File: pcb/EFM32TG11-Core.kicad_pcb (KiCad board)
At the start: 2 copper layers, 76.2 x 45.7 mm, 53 parts, among them J1 PWR_IN, J2 EXT_PWR, J3 EXT_UART, J4 EXT_I2C, J5 BOOT, J6 Conn_ARM_JTAG_SWD_10, J7 GPIO_HI, J8 GPIO_LO, Q1 Si2301CDS, SW1 SW_Push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

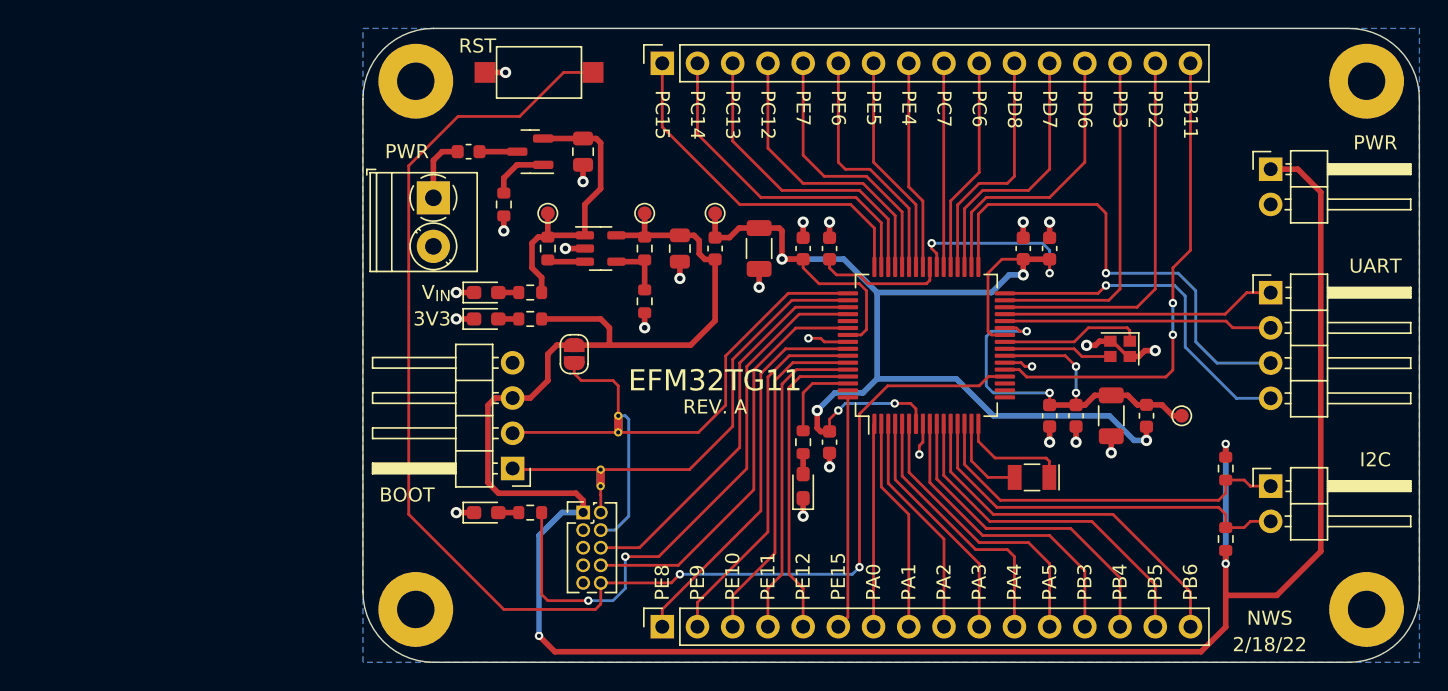
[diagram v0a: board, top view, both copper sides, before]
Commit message: Reorganization of schematic to heirarchical sheets
Took single sheet schematic and reorganized to 3 heirarchical sheets.
This allowed for the schematic to be printable on 8.5"x11" sheets of
paper without losing clarity of the schematic. All reference
designators were maintained.

Buses and interconnects between pages still need to be added to the
schematic to finish transition.

[Issue: X]
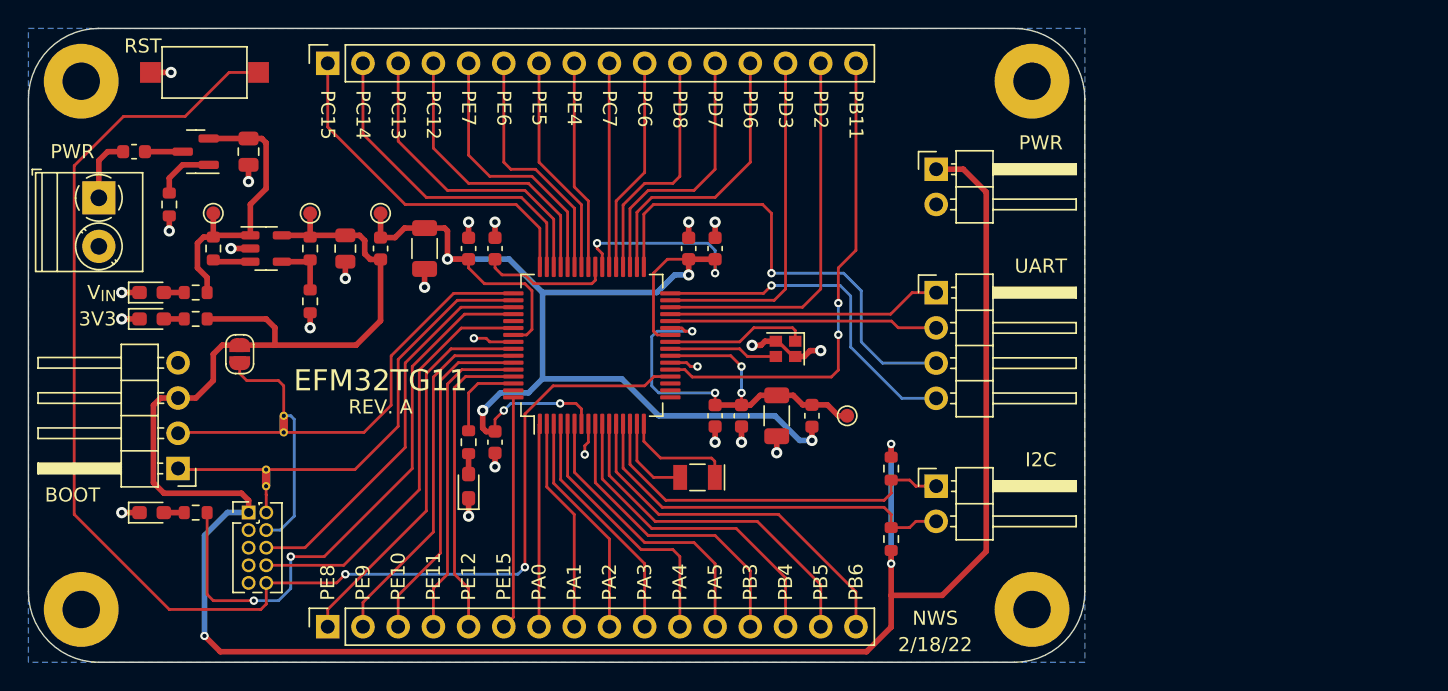
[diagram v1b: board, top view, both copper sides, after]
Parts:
- J7: value GPIO_HI -> GPIO_LO
- J8: value GPIO_LO -> GPIO_HI
- R10, R9: value 4.7k -> 4k7
- R2, R4, R7, R8: value 2.2k -> 2k2
- R3: value 2.0M -> 2M
- R6: value 1.2M -> 1M2
- moved FB2 24.1 mm to (151.8, 106.7)
- moved H3 24.1 mm to (167.6, 82.5)
- moved H4 24.1 mm to (167.6, 120.7)
- moved R10 24.1 mm to (157.5, 110.5)
- moved R9 24.1 mm to (157.5, 115.6)
- moved U2 24.1 mm to (135.9, 101.6)
- moved C2 24.1 mm to (118.1, 94.6)
- moved C3 24.1 mm to (123.8, 94.6)
- moved D1 24.1 mm to (104.1, 97.8)
- moved D2 24.1 mm to (104.1, 99.7)
- moved D3 24.1 mm to (104.1, 113.7)
- moved J5 24.1 mm to (106.0, 110.5)
- moved JP1 24.1 mm to (110.5, 102.2)
- moved NT2 24.1 mm to (112.4, 111.8)
- moved R1 24.1 mm to (108.6, 94.6)
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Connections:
- net /BTLDR renamed /MCU/BTLDR
- net /HFXTALN renamed /MCU/HFXTALN
- net /HFXTALP renamed /MCU/HFXTALP
- net /LFXTALN renamed /MCU/LFXTALN
- net /LFXTALP renamed /MCU/LFXTALP
- net /PA12 renamed /MCU/PA12
- net /PA13 renamed /MCU/PA13
- net /PA14 renamed /MCU/PA14
- net /PE14 renamed /MCU/PE14
- net /RX_{BOOT} renamed /MCU/RX_{BOOT}
- net /SWCLK renamed /MCU/SWCLK
- net /SWDIO renamed /MCU/SWDIO
- net /TDI_{JTAG} renamed /MCU/TDI_{JTAG}
- net /TDO_{JTAG} renamed /MCU/TDO_{JTAG}
- net /TX_{BOOT} renamed /MCU/TX_{BOOT}
- net /USR renamed /MCU/USR
- net /~{RST} renamed /MCU/~{RST}
- J3 pad 1: /UART1_{RX} -> /IO Connectors/UART1_{RX}
- J3 pad 2: /UART1_{TX} -> /IO Connectors/UART1_{TX}
- J3 pad 3: /UART1_{RTS} -> /IO Connectors/UART1_{RTS}
- J3 pad 4: /UART1_{CTS} -> /IO Connectors/UART1_{CTS}
- J4 pad 1: /I2C1_{SCL} -> /IO Connectors/I2C1_{SCL}
- J4 pad 2: /I2C1_{SDA} -> /IO Connectors/I2C1_{SDA}
- J7 pad 1: /PE8 -> /IO Connectors/PE8
- J7 pad 10: /PA3 -> /IO Connectors/PA3
- J7 pad 11: /PA4 -> /IO Connectors/PA4
- J7 pad 12: /PA5 -> /IO Connectors/PA5
- J7 pad 13: /PB3 -> /IO Connectors/PB3
- J7 pad 14: /PB4 -> /IO Connectors/PB4
- J7 pad 15: /PB5 -> /IO Connectors/PB5
- J7 pad 16: /PB6 -> /IO Connectors/PB6
- J7 pad 2: /PE9 -> /IO Connectors/PE9
- J7 pad 3: /PE10 -> /IO Connectors/PE10
- J7 pad 4: /PE11 -> /IO Connectors/PE11
- J7 pad 5: /PE12 -> /IO Connectors/PE12
- J7 pad 6: /PE15 -> /IO Connectors/PE15
- J7 pad 7: /PA0 -> /IO Connectors/PA0
- J7 pad 8: /PA1 -> /IO Connectors/PA1
- J7 pad 9: /PA2 -> /IO Connectors/PA2
- J8 pad 1: /PC15 -> /IO Connectors/PC15
- J8 pad 10: /PC6 -> /IO Connectors/PC6
- J8 pad 11: /PD8 -> /IO Connectors/PD8
- J8 pad 12: /PD7 -> /IO Connectors/PD7
- J8 pad 13: /PD6 -> /IO Connectors/PD6
- J8 pad 14: /PD3 -> /IO Connectors/PD3
- J8 pad 15: /PD2 -> /IO Connectors/PD2
- J8 pad 16: /PB11 -> /IO Connectors/PB11
- J8 pad 2: /PC14 -> /IO Connectors/PC14
- J8 pad 3: /PC13 -> /IO Connectors/PC13
- J8 pad 4: /PC12 -> /IO Connectors/PC12
- J8 pad 5: /PE7 -> /IO Connectors/PE7
- J8 pad 6: /PE6 -> /IO Connectors/PE6
- J8 pad 7: /PE5 -> /IO Connectors/PE5
- J8 pad 8: /PE4 -> /IO Connectors/PE4
- J8 pad 9: /PC7 -> /IO Connectors/PC7
- R10 pad 2: /I2C1_{SCL} -> /IO Connectors/I2C1_{SCL}
- R9 pad 2: /I2C1_{SDA} -> /IO Connectors/I2C1_{SDA}
- U2 pad 1: /PA0 -> /MCU/PA0
- U2 pad 10: /PB4 -> /MCU/PB4
- U2 pad 11: /PB5 -> /MCU/PB5
- U2 pad 12: /PB6 -> /MCU/PB6
- U2 pad 13: /I2C1_{SDA} -> /MCU/I2C1_{SDA}
- U2 pad 14: /I2C1_{SCL} -> /MCU/I2C1_{SCL}
- U2 pad 2: /PA1 -> /MCU/PA1
- U2 pad 21: /PB11 -> /MCU/PB11
- U2 pad 28: /UART1_{TX} -> /MCU/UART1_{TX}
- U2 pad 29: /UART1_{RX} -> /MCU/UART1_{RX}
- U2 pad 3: /PA2 -> /MCU/PA2
- U2 pad 30: /PD2 -> /MCU/PD2
- U2 pad 31: /PD3 -> /MCU/PD3
- U2 pad 32: /UART1_{CTS} -> /MCU/UART1_{CTS}
- U2 pad 33: /UART1_{RTS} -> /MCU/UART1_{RTS}
- U2 pad 34: /PD6 -> /MCU/PD6
- U2 pad 35: /PD7 -> /MCU/PD7
- U2 pad 36: /PD8 -> /MCU/PD8
- U2 pad 37: /PC6 -> /MCU/PC6
- U2 pad 38: /PC7 -> /MCU/PC7
- U2 pad 4: /PA3 -> /MCU/PA3
- U2 pad 41: /PE4 -> /MCU/PE4
- U2 pad 42: /PE5 -> /MCU/PE5
- U2 pad 43: /PE6 -> /MCU/PE6
- U2 pad 44: /PE7 -> /MCU/PE7
- U2 pad 45: /PC12 -> /MCU/PC12
- U2 pad 46: /PC13 -> /MCU/PC13
- U2 pad 47: /PC14 -> /MCU/PC14
- U2 pad 48: /PC15 -> /MCU/PC15
- U2 pad 5: /PA4 -> /MCU/PA4
- U2 pad 53: unconnected-(U2-Pad53) -> /MCU/PF4
- U2 pad 57: /PE8 -> /MCU/PE8
- U2 pad 58: /PE9 -> /MCU/PE9
- U2 pad 59: /PE10 -> /MCU/PE10
- U2 pad 6: /PA5 -> /MCU/PA5
- U2 pad 60: /PE11 -> /MCU/PE11
- U2 pad 61: /PE12 -> /MCU/PE12
- U2 pad 64: /PE15 -> /MCU/PE15
- U2 pad 9: /PB3 -> /MCU/PB3
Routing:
- net /PB11: track 35.2 -> 0.00 mm, vias 2 -> 0
- net /IO Connectors/PB11: track 0.00 -> 35.2 mm, vias 0 -> 2
- net /MCU/UART1_{RTS}: track 0.00 -> 34.6 mm, vias 0 -> 1
- net /UART1_{RTS}: track 34.6 -> 0.00 mm, vias 1 -> 0
- net /IO Connectors/I2C1_{SDA}: track 0.00 -> 28.3 mm
- net /I2C1_{SDA}: track 28.3 -> 0.00 mm
- net /MCU/PE8: track 0.00 -> 28.2 mm
- net /PE8: track 28.2 -> 0.00 mm
- net /PD2: track 27.7 -> 0.00 mm
- net /IO Connectors/PD2: track 0.00 -> 27.7 mm
- net /IO Connectors/I2C1_{SCL}: track 0.00 -> 27.4 mm
- net /I2C1_{SCL}: track 27.4 -> 0.00 mm
- net /IO Connectors/PB6: track 0.00 -> 26.9 mm
- net /PB6: track 26.9 -> 0.00 mm
- net /MCU/PE9: track 0.00 -> 26.5 mm
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
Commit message: Fix Nets for Hierarchical Sheets
Defined busses to pass nets to and from MCU sheet and IO connector
sheet.
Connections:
- U2 pad 17: /MCU/PA12 -> unconnected-(U2-Pad17)
- U2 pad 18: /MCU/PA13 -> unconnected-(U2-Pad18)
- U2 pad 19: /MCU/PA14 -> unconnected-(U2-Pad19)
- U2 pad 28: /MCU/UART1_{TX} -> /IO Connectors/UART1_{TX}
- U2 pad 29: /MCU/UART1_{RX} -> /IO Connectors/UART1_{RX}
- U2 pad 32: /MCU/UART1_{CTS} -> /IO Connectors/UART1_{CTS}
- U2 pad 33: /MCU/UART1_{RTS} -> /IO Connectors/UART1_{RTS}
- U2 pad 53: /MCU/PF4 -> unconnected-(U2-Pad53)
- U2 pad 63: /MCU/PE14 -> unconnected-(U2-Pad63)
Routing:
- net /MCU/PB11: track 0.00 -> 35.2 mm, vias 0 -> 2
- net /IO Connectors/PB11: track 35.2 -> 0.00 mm, vias 2 -> 0
- net /MCU/UART1_{RTS}: track 34.6 -> 0.00 mm, vias 1 -> 0
- net /IO Connectors/UART1_{RTS}: track 0.00 -> 34.6 mm, vias 0 -> 1
- net /MCU/PE8: track 28.2 -> 0.00 mm
- net /IO Connectors/PE8: track 0.00 -> 28.2 mm
- net /MCU/PD2: track 0.00 -> 27.7 mm
- net /IO Connectors/PD2: track 27.7 -> 0.00 mm
- net /MCU/PC15: track 0.00 -> 25.7 mm
- net /IO Connectors/PC15: track 25.7 -> 0.00 mm
- net /MCU/PB5: track 25.3 -> 0.00 mm
- net /IO Connectors/PB5: track 0.00 -> 25.3 mm
- net /MCU/UART1_{CTS}: track 24.9 -> 0.00 mm, vias 1 -> 0
- net /IO Connectors/UART1_{CTS}: track 0.00 -> 24.9 mm, vias 0 -> 1
- net /MCU/PD3: track 0.00 -> 24.9 mm
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
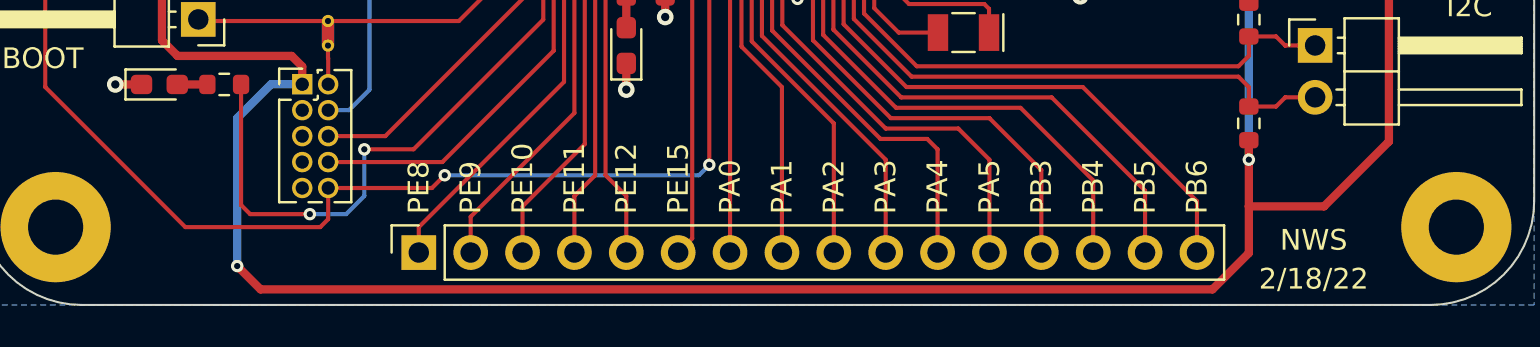
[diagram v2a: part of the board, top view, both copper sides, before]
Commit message: Added commit hash to schematic and PCB
Commit hash was added as a text variable to be added to the schematic
title block and the PCB silkscreen layer. A box with label to record
the board # was also added to the PCB silkscreen layer.

[Issue: X]
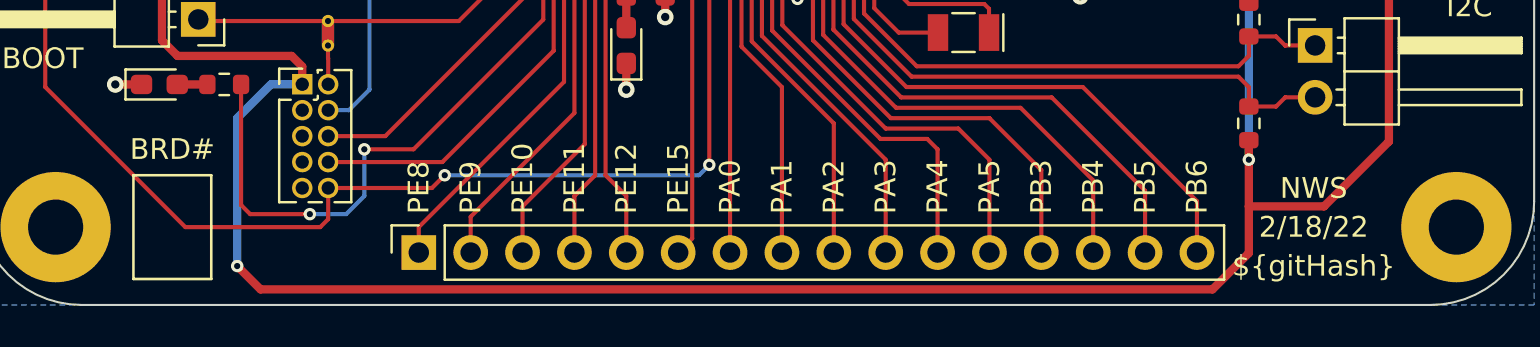
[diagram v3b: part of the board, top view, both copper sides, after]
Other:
- board text added: "${gitHash}"
- board text added: "BRD#"
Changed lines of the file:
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@@
     )
   )
+  (property "gitHash" "20d7c9d")
   (net 0 "")
   (net 1 "Net-(C1-Pad1)")
@@
     )
   )
+  (gr_rect (start 102.87 118.11) (end 106.68 123.19) (layer "F.SilkS") (width 0.127) (fill none))
   (gr_line (start 171.45 83.82) (end 171.45 119.38) (layer "Edge.Cuts") (width 0.1))
   (gr_arc (start 100.33 124.46) (mid 96.737898 122.972102) (end 95.25 119.38) (layer "Edge.Cuts") (width 0.1))
@@
     (effects (font (size 1.016 1.016) (thickness 0.1524)) (justify left))
   )
+  (gr_text "${gitHash}" (at 160.655 122.555) (layer "F.SilkS")
+    (effects (font (size 1.016 1.016) (thickness 0.1524)))
+  )
   (gr_text "PA2" (at 137.16 120.015 90) (layer "F.SilkS")
     (effects (font (size 1.016 1.016) (thickness 0.1524)) (justify left))
@@
     (effects (font (size 1.016 1.016) (thickness 0.1524)))
   )
-  (gr_text "NWS" (at 160.655 121.285) (layer "F.SilkS")
+  (gr_text "NWS" (at 160.655 118.745) (layer "F.SilkS")
     (effects (font (size 1.016 1.016) (thickness 0.1524)))
   )
@@
     (effects (font (size 1.016 1.016) (thickness 0.1524)))
   )
+  (gr_text "BRD#" (at 104.775 116.84) (layer "F.SilkS")
+    (effects (font (size 1.016 1.016) (thickness 0.1524)))
+  )
   (gr_text "PE11" (at 124.46 120.015 90) (layer "F.SilkS")
     (effects (font (size 1.016 1.016) (thickness 0.1524)) (justify left))
@@
     (effects (font (size 1.016 1.016) (thickness 0.1524)))
   )
-  (gr_text "2/18/22" (at 160.655 123.19) (layer "F.SilkS")
+  (gr_text "2/18/22" (at 160.655 120.65) (layer "F.SilkS")
     (effects (font (size 1.016 1.016) (thickness 0.1524)))
   )
